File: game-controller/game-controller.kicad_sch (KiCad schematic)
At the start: 20 parts, among them J1 Conn_01x22, J10 Conn_01x01, J11 Conn_01x01, J12 Conn_01x01, J13 Conn_01x01, J14 Conn_01x01, J15 Conn_01x01, J16 Conn_01x01, J2 Conn_01x22, J3 Conn_01x01, J4 Conn_01x01, J5 Conn_01x01, J6 Conn_01x01, J7 Conn_01x01, J8 Conn_01x01, J9 Conn_01x01

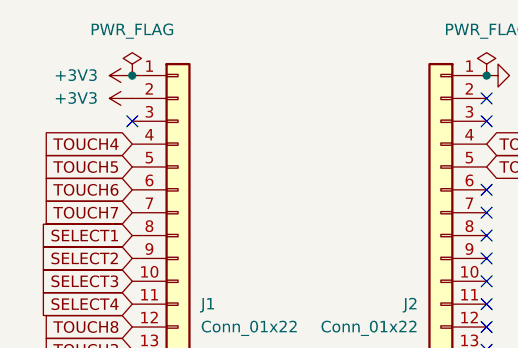
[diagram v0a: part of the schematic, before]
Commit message: Delete +3V3 from 4 dev boards
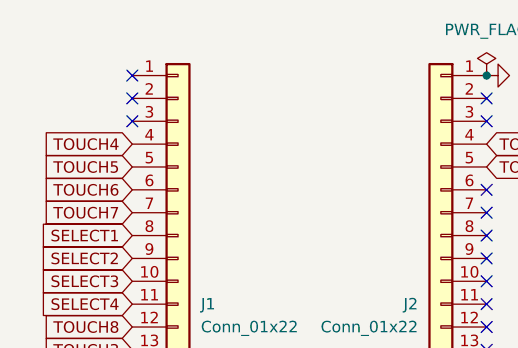
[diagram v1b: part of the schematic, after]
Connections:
- net +3V3: no longer names the net of J1.1 (Pin_1)
- net +3V3: no longer J1.2 (Pin_2)
- no-connect marks 28 -> 30
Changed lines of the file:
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@@
 	(paper "A4")
 	(junction
-		(at 54.61 68.58)
-		(diameter 0)
-		(color 0 0 0 0)
-	)
-	(junction
 		(at 93.98 68.58)
 		(diameter 0)
@@
 	)
 	(no_connect
+		(at 54.61 71.12)
+	)
+	(no_connect
 		(at 241.3 114.3)
 	)
@@
 	)
 	(no_connect
+		(at 54.61 68.58)
+	)
+	(no_connect
 		(at 241.3 102.87)
 	)
@@
 	)
 	(symbol
-		(lib_id "power:+3V3")
-		(at 54.61 68.58 90)
-		(unit 1)
-		(exclude_from_sim no)
-		(in_bom yes)
-		(on_board yes)
-		(dnp no)
-		(fields_autoplaced yes)
-		(property "Reference" "#PWR01"
-			(at 58.42 68.58 0)
-			(effects
-				(font
-					(size 1.27 1.27)
-				)
-				(hide yes)
-			)
-		)
-		(property "Value" "+3V3"
-			(at 50.8 68.5799 90)
-			(effects
-				(font
-					(size 1.27 1.27)
-				)
-				(justify left)
-			)
-		)
-		(property "Footprint" ""
-			(at 54.61 68.58 0)
-			(effects
-				(font
-					(size 1.27 1.27)
-				)
-				(hide yes)
-			)
-		)
-		(property "Datasheet" ""
-			(at 54.61 68.58 0)
-			(effects
-				(font
-					(size 1.27 1.27)
-				)
-				(hide yes)
-			)
-		)
-		(property "Description" "Power symbol creates a global label with name \"+3V3\""
-			(at 54.61 68.58 0)
-			(effects
-				(font
-					(size 1.27 1.27)
-				)
-				(hide yes)
-			)
-		)
-		(pin "1"
-		)
-		(instances
-			(project "game-controller"
-				(path "/884d4743-baec-4dea-9c6f-bf16a0e97810"
-					(reference "#PWR01")
-					(unit 1)
-				)
-			)
-		)
-	)
-	(symbol
 		(lib_id "power:GND")
 		(at 93.98 68.58 90)
@@
 	)
 	(symbol
-		(lib_id "power:PWR_FLAG")
-		(at 54.61 68.58 0)
-		(unit 1)
-		(exclude_from_sim no)
-		(in_bom yes)
-		(on_board yes)
-		(dnp no)
-		(fields_autoplaced yes)
-		(property "Reference" "#FLG01"
-			(at 54.61 66.675 0)
-			(effects
-				(font
-					(size 1.27 1.27)
-				)
-				(hide yes)
-			)
-		)
-		(property "Value" "PWR_FLAG"
-			(at 54.61 63.5 0)
-			(effects
-				(font
-					(size 1.27 1.27)
-				)
-			)
-		)
-		(property "Footprint" ""
-			(at 54.61 68.58 0)
-			(effects
-				(font
-					(size 1.27 1.27)
-				)
-				(hide yes)
-			)
-		)
-		(property "Datasheet" "~"
-			(at 54.61 68.58 0)
-			(effects
-				(font
-					(size 1.27 1.27)
-				)
-				(hide yes)
-			)
-		)
-		(property "Description" "Special symbol for telling ERC where power comes from"
-			(at 54.61 68.58 0)
-			(effects
-				(font
-					(size 1.27 1.27)
-				)
-				(hide yes)
-			)
-		)
-		(pin "1"
-		)
-		(instances
-			(project "game-controller"
-				(path "/884d4743-baec-4dea-9c6f-bf16a0e97810"
-					(reference "#FLG01")
-					(unit 1)
-				)
-			)
-		)
-	)
-	(symbol
 		(lib_id "Connector_Generic:Conn_01x01")
 		(at 171.45 88.9 270)
@@
 					(unit 1)
 				)
-			)
-		)
-	)
-	(symbol
-		(lib_id "power:+3V3")
-		(at 54.61 71.12 90)
-		(unit 1)
-		(exclude_from_sim no)
-		(in_bom yes)
-		(on_board yes)
-		(dnp no)
-		(fields_autoplaced yes)
-		(property "Reference" "#PWR02"
-			(at 58.42 71.12 0)
-			(effects
-				(font
-					(size 1.27 1.27)
-				)
-				(hide yes)
-			)
-		)
-		(property "Value" "+3V3"
-			(at 50.8 71.1199 90)
-			(effects
-				(font
-					(size 1.27 1.27)
-				)
-				(justify left)
-			)
-		)
-		(property "Footprint" ""
-			(at 54.61 71.12 0)
-			(effects
-				(font
-					(size 1.27 1.27)
-				)
-				(hide yes)
-			)
-		)
-		(property "Datasheet" ""
-			(at 54.61 71.12 0)
-			(effects
-				(font
-					(size 1.27 1.27)
-				)
-				(hide yes)
-			)
-		)
-		(property "Description" "Power symbol creates a global label with name \"+3V3\""
-			(at 54.61 71.12 0)
-			(effects
-				(font
-					(size 1.27 1.27)
-				)
-				(hide yes)
-			)
-		)
-		(pin "1"
-		)
-		(instances
-			(project "game-controller"
-				(path "/884d4743-baec-4dea-9c6f-bf16a0e97810"
-					(reference "#PWR02")
-					(unit 1)
-				)
